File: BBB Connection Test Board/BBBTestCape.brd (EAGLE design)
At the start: 49.5 x 47.9 mm, 22 parts, among them X1 SWTCH_BLCK, X2 SWTCH_BLCK

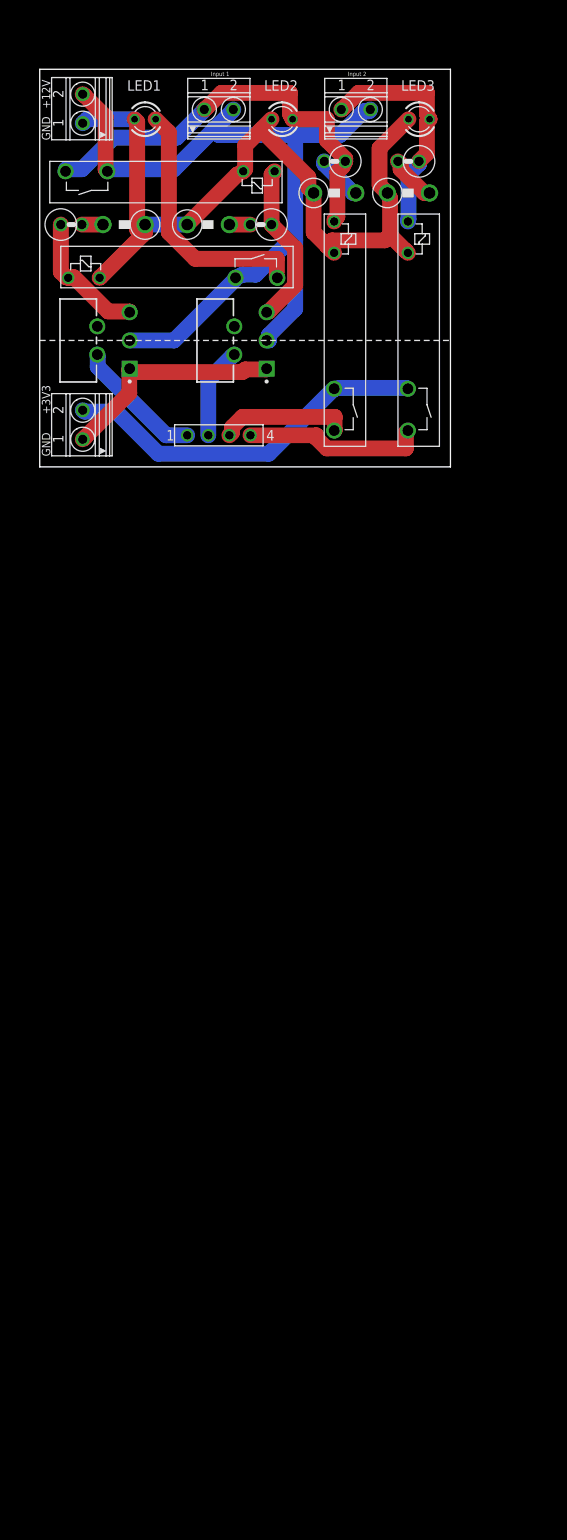
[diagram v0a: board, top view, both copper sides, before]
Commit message: WIP: Starting BBB Connection Test Board rev B. Added MCP23017
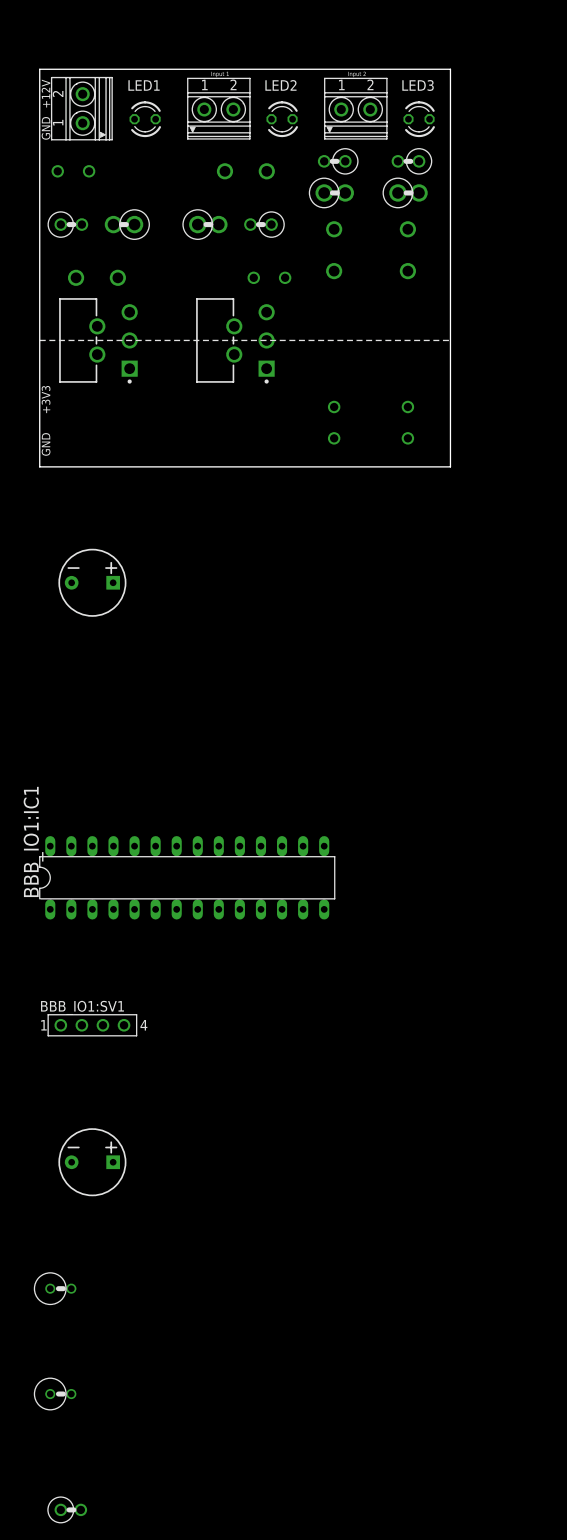
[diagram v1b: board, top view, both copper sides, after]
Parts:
- removed 3V3_PWR_BLK:PWR: PWR_BLK, relay_computer_custom:1751248
- removed SV1: (no value), relay_computer_custom:FE04-1
- added 12V_PWR_BLK:C1, BBB_IO1:C1: 100uF, relay_computer_custom:CPOL-RADIAL-5MM-8MM
- added BBB_IO1:C2: 0.1UF, relay_computer_custom:VERT_CAP
- added BBB_IO1:IC1: MCP23017SP, relay_computer_custom:DIL28-3
- added BBB_IO1:R1, BBB_IO1:R2: 4.7KOHM, relay_computer_custom:RAD2.5_RES
- added BBB_IO1:SV1: (no value), relay_computer_custom:FE04-1
- 12V_TO_3V3_1BIT1:D6, 3V3_TO_12_1BIT1:D4, DUAL_12V⇆3V3_1BIT1:12V_TO_3V3_1BIT1:D6, DUAL_12V⇆3V3_1BIT1:3V3_TO_12_1BIT1:D4: value 1N5359 -> 1N5359VERT_SML; device relay_computer_custom:C1702-05 -> relay_computer_custom:RAD2.5_D2
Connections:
- removed net BBB1: 3V3_TO_12_1BIT1:U1.2, SV1.1
- removed net BBB2: DUAL_12V⇆3V3_1BIT1:3V3_TO_12_1BIT1:U1.2, SV1.2
- removed net BBB3: DUAL_12V⇆3V3_1BIT1:12V_TO_3V3_1BIT1:K3.5, SV1.3
- removed net BBB4: 12V_TO_3V3_1BIT1:K3.5, SV1.4
- new net BBB_IO1:SCL: BBB_IO1:IC1.12, BBB_IO1:R1.C, BBB_IO1:SV1.3
- new net BBB_IO1:SDA: BBB_IO1:IC1.13, BBB_IO1:R2.C, BBB_IO1:SV1.4
- new net N$4: BBB_IO1:IC1.8, DUAL_12V⇆3V3_1BIT1:3V3_TO_12_1BIT1:U1.2
- new net N$5: BBB_IO1:IC1.1, DUAL_12V⇆3V3_1BIT1:12V_TO_3V3_1BIT1:K3.5
- new net N$6: 3V3_TO_12_1BIT1:U1.2, BBB_IO1:IC1.28
- new net N$7: 12V_TO_3V3_1BIT1:K3.5, BBB_IO1:IC1.21
- net +12V: now also 12V_PWR_BLK:C1.1
- net +3V3: now also BBB_IO1:C1.1, BBB_IO1:C2.A, BBB_IO1:IC1.18, BBB_IO1:IC1.9, BBB_IO1:R1.A, BBB_IO1:R2.A, BBB_IO1:SV1.1; no longer 3V3_PWR_BLK:PWR.2
- net GND: now also 12V_PWR_BLK:C1.2
- net GND3: now also BBB_IO1:C1.2, BBB_IO1:C2.C, BBB_IO1:IC1.10, BBB_IO1:IC1.15, BBB_IO1:IC1.16, BBB_IO1:IC1.17, BBB_IO1:SV1.2; no longer 3V3_PWR_BLK:PWR.1
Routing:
- net +12V: track 100.6 -> 0.00 mm
- net GND: track 97.2 -> 0.00 mm
- net N$3: track 52.2 -> 0.00 mm
- net +3V3: track 44.6 -> 0.00 mm
- net N$1: track 31.0 -> 0.00 mm
- net N$2: track 27.8 -> 0.00 mm
- net GND3: track 27.7 -> 0.00 mm
- net BBB4: track 21.8 -> 0.00 mm
- net DUAL_12V⇆3V3_1BIT1:3V3_TO_12_1BIT1:N$1: track 19.8 -> 0.00 mm
- net 3V3_TO_12_1BIT1:N$1: track 16.1 -> 0.00 mm
- net BBB1: track 15.7 -> 0.00 mm
- net BBB3: track 15.7 -> 0.00 mm
- net BBB2: track 11.0 -> 0.00 mm
- net 12V_TO_3V3_1BIT1:D$3: track 5.76 -> 0.00 mm
- net DUAL_12V⇆3V3_1BIT1:12V_TO_3V3_1BIT1:D$3: track 5.57 -> 0.00 mm
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
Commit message: WIP: starting layout of BBB conn. test board rev B
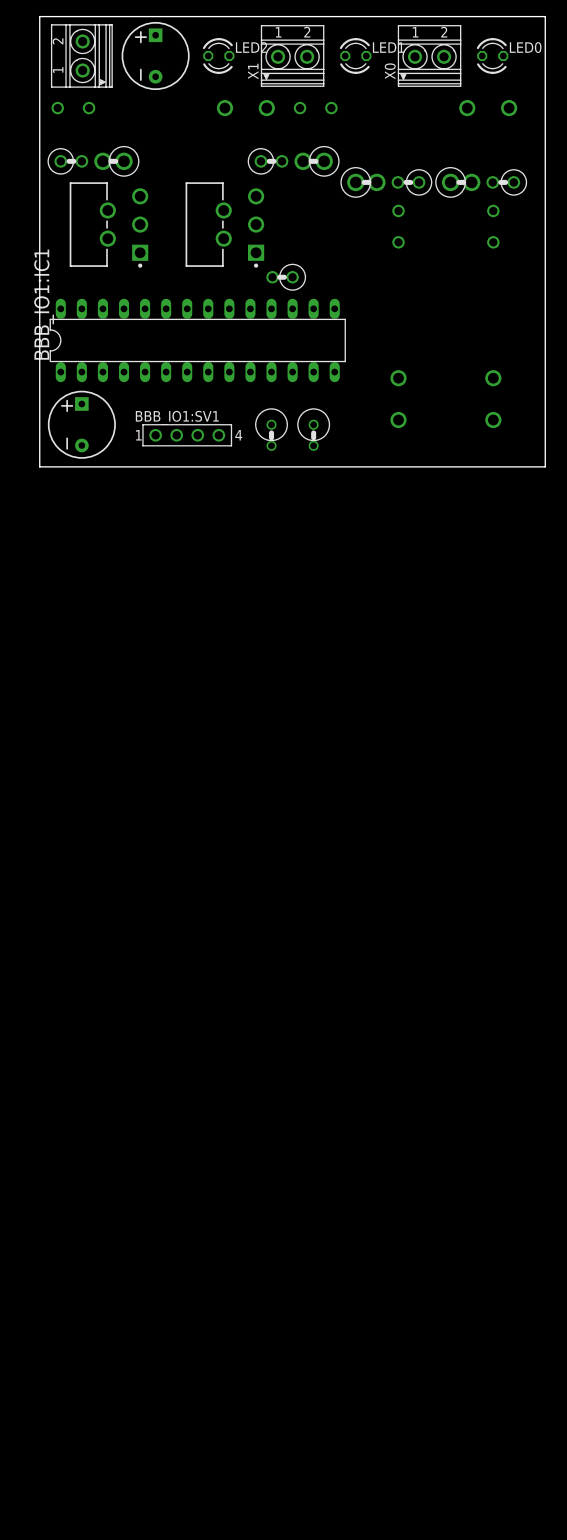
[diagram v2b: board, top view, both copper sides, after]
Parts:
- removed LED3: (no value), relay_computer_custom:LED3MM
- removed X2: SWTCH_BLCK, relay_computer_custom:1751248
- added LED0: (no value), relay_computer_custom:LED3MM
- added X0: SWTCH_BLCK, relay_computer_custom:1751248
- moved BBB_IO1:C2 150.7 mm to (29.2, 22.9), turned to 180 degrees
- moved BBB_IO1:R2 119.5 mm to (33.0, 3.81), turned to 270 degrees
- moved BBB_IO1:R1 106.0 mm to (27.9, 3.81), turned to 270 degrees
- moved BBB_IO1:C1 88.9 mm to (5.08, 5.08), turned to 90 degrees
- moved BBB_IO1:SV1 72.0 mm to (17.8, 3.81)
- moved BBB_IO1:IC1 64.8 mm to (19.1, 15.2)
- moved 12V_PWR_BLK:C1 64.0 mm to (14.0, 49.5), turned to 90 degrees
- moved 3V3_TO_12_1BIT1:K2 60.4 mm to (58.4, 44.5), turned to 180 degrees
- moved 3V3_TO_12_1BIT1:D3 41.0 mm to (44.5, 34.3), turned to 180 degrees
- moved 3V3_TO_12_1BIT1:D4 29.6 mm to (39.4, 34.3), turned to 0 degrees
- moved 12V_TO_3V3_1BIT1:K3 29.5 mm to (55.9, 3.81), turned to 90 degrees
- moved DUAL_12V⇆3V3_1BIT1:12V_TO_3V3_1BIT1:K3 28.5 mm to (44.5, 3.81), turned to 90 degrees
- moved LED1 26.5 mm to (38.1, 49.5), turned to 0 degrees
- moved DUAL_12V⇆3V3_1BIT1:3V3_TO_12_1BIT1:D3 24.1 mm to (3.81, 36.8), turned to 0 degrees
- moved 3V3_TO_12_1BIT1:U1 20.7 mm to (24.1, 29.2)
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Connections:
- net +12V: now also X0.2; no longer X2.2
- net GND: now also LED0.K; no longer LED3.K
- net N$2: now also LED0.A, X0.1; no longer LED3.A, X2.1
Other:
- board size 49.5 x 47.9 mm -> 60.9 x 54.3 mm
- board text removed: "+12V"
- board text removed: "+3V3"
- board text removed: "BBB Test Board Rev A"
- board text removed: "GND"
- board text removed: "Input 1"
- board text removed: "Input 2"

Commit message: Almost finished with Rev B of connector board. Comestic changes only
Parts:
- moved DUAL_12V⇆3V3_1BIT1:3V3_TO_12_1BIT1:D3 27.9 mm to (29.2, 25.4), turned to 180 degrees
- moved DUAL_12V⇆3V3_1BIT1:3V3_TO_12_1BIT1:D4 21.7 mm to (29.2, 29.2), turned to 0 degrees
- moved DUAL_12V⇆3V3_1BIT1:12V_TO_3V3_1BIT1:D5 14.5 mm to (36.8, 25.4)
- moved 3V3_TO_12_1BIT1:D4 13.2 mm to (47.0, 23.5), turned to 90 degrees
- moved 12V_TO_3V3_1BIT1:D6 12.5 mm to (57.1, 23.5), turned to 90 degrees
- moved DUAL_12V⇆3V3_1BIT1:12V_TO_3V3_1BIT1:D6 8.03 mm to (35.6, 29.2)
- moved 12V_PWR_BLK:C1 7.62 mm to (14.0, 41.9)
- moved 12V_PWR_BLK:PWR 7.62 mm to (5.08, 41.9)
- moved 3V3_TO_12_1BIT1:K2 7.62 mm to (58.4, 36.8)
- moved DUAL_12V⇆3V3_1BIT1:3V3_TO_12_1BIT1:K2 7.62 mm to (29.2, 36.8)
- moved LED0 7.62 mm to (54.6, 41.9), turned to 270 degrees
- moved LED1 7.62 mm to (38.1, 41.9), turned to 270 degrees
- moved LED2 7.62 mm to (21.6, 41.9), turned to 270 degrees
- moved X0 7.62 mm to (47.0, 41.9)
- moved X1 7.62 mm to (30.5, 41.9)
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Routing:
- net N$5: track 0.00 -> 45.5 mm
- net N$3: track 0.00 -> 44.9 mm
- net DUAL_12V⇆3V3_1BIT1:3V3_TO_12_1BIT1:N$1: track 0.00 -> 39.8 mm
- net N$7: track 0.00 -> 37.6 mm
- net N$4: track 0.00 -> 31.9 mm
- net 3V3_TO_12_1BIT1:N$1: track 0.00 -> 30.4 mm
- net N$6: track 0.00 -> 29.5 mm
- net N$2: track 0.00 -> 28.2 mm
- net N$1: track 0.00 -> 21.6 mm
- net BBB_IO1:SDA: track 0.00 -> 18.8 mm
- net BBB_IO1:SCL: track 0.00 -> 16.5 mm
- net DUAL_12V⇆3V3_1BIT1:12V_TO_3V3_1BIT1:D$3: track 0.00 -> 10.5 mm
- net DUAL_12V⇆3V3_1BIT1:3V3_TO_12_1BIT1:D$2: track 0.00 -> 4.86 mm
- net 3V3_TO_12_1BIT1:D$2: track 0.00 -> 2.54 mm
- net 12V_TO_3V3_1BIT1:D$3: track 0.00 -> 2.54 mm
- added copper zone on layer 15, net +12V
- added copper zone on layer 15, net +3V3
- added copper zone on layer 2, net GND
- added copper zone on layer 2, net GND3
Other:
- board size 60.9 x 54.3 mm -> 59.7 x 46.7 mm
- board text added: "12V"
- board text added: "3.3V"
- board text added: "GND"
- board text added: "SCL"
- board text added: "SDA"

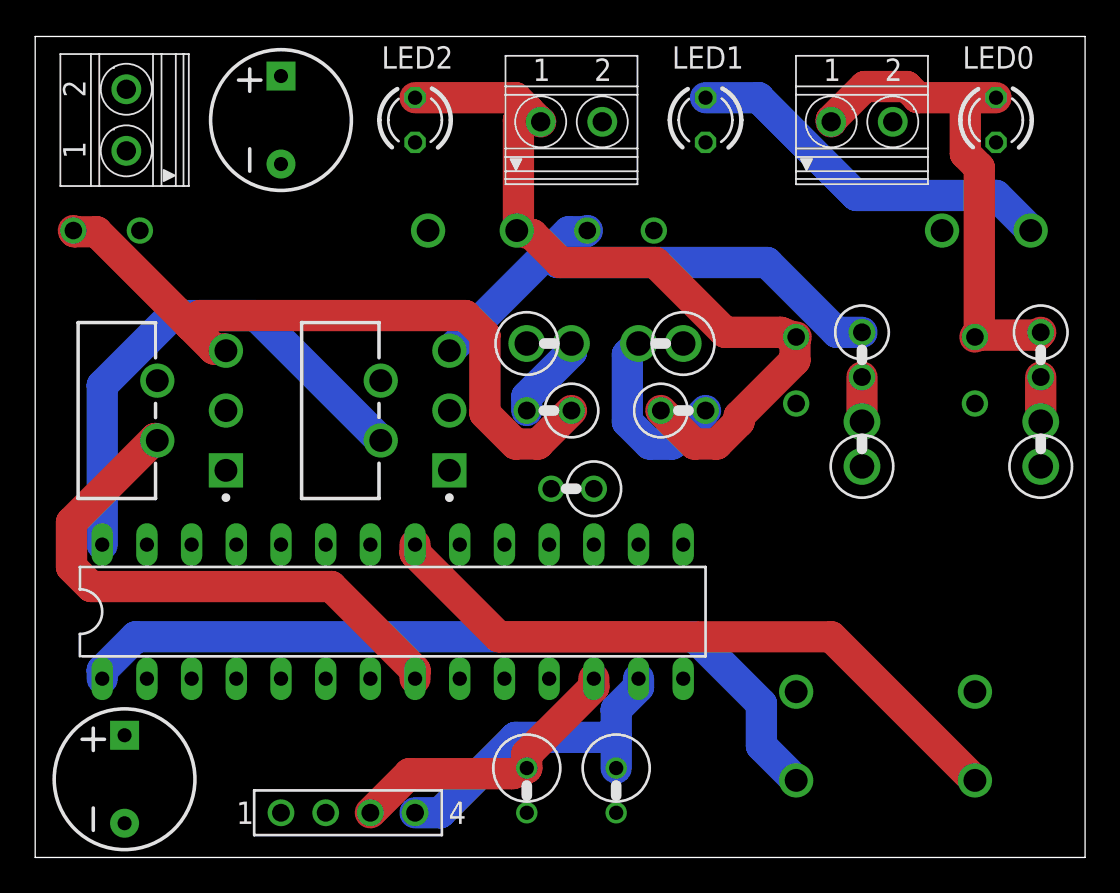
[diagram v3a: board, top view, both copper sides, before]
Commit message: Adding pull down resistors for inputs to MCP23017
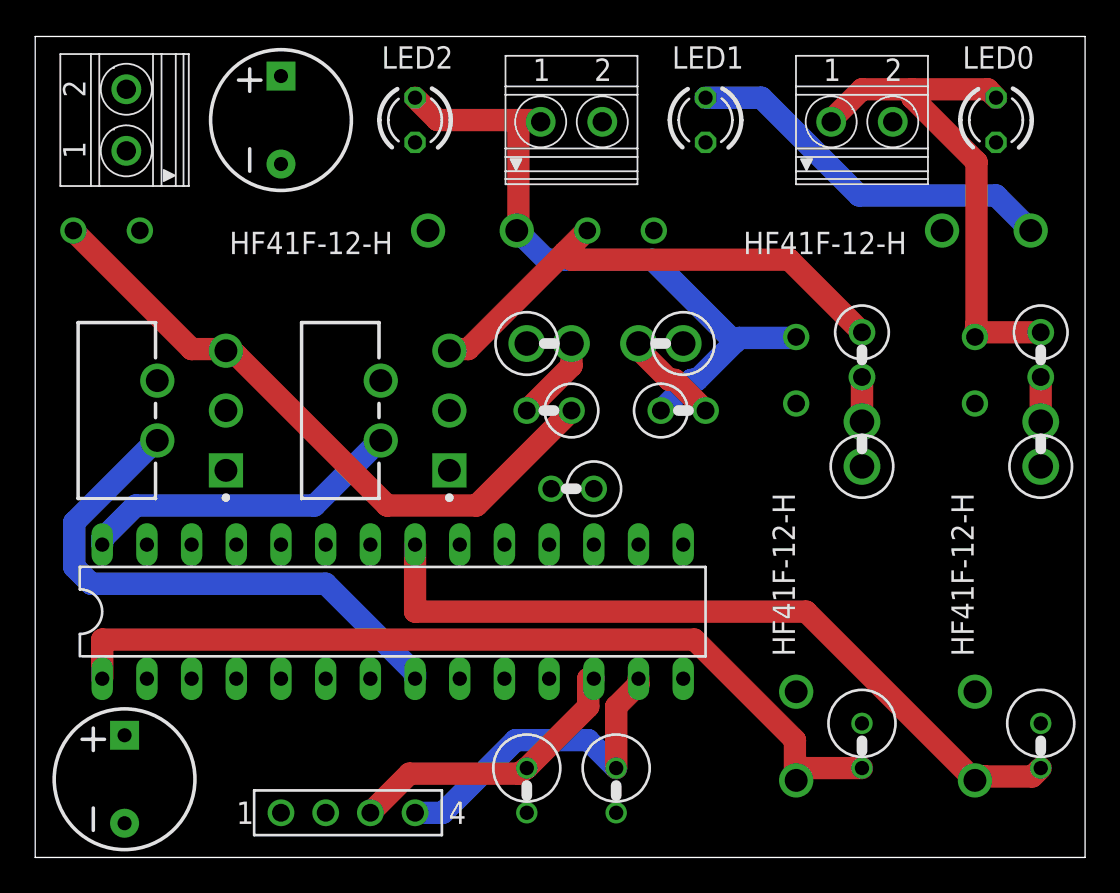
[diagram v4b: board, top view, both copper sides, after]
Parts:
- added BBB_IO1:R3, BBB_IO1:R4: 4.7KOHM, relay_computer_custom:RAD2.5_RES
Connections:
- net GND3: now also BBB_IO1:R3.C, BBB_IO1:R4.C
- net N$5: now also BBB_IO1:R4.A
- net N$7: now also BBB_IO1:R3.A
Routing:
- net N$6: track 29.5 -> 18.5 mm
- net N$3: track 44.9 -> 38.5 mm
- net N$7: track 37.6 -> 43.6 mm
- net N$5: track 45.5 -> 50.4 mm
- net DUAL_12V⇆3V3_1BIT1:12V_TO_3V3_1BIT1:D$3: track 10.5 -> 5.57 mm
- net DUAL_12V⇆3V3_1BIT1:3V3_TO_12_1BIT1:N$1: track 39.8 -> 37.0 mm
- net N$2: track 28.2 -> 29.8 mm
- net 3V3_TO_12_1BIT1:N$1: track 30.4 -> 29.4 mm
- net BBB_IO1:SDA: track 18.8 -> 19.4 mm
- net N$4: track 31.9 -> 31.4 mm

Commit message: Finishing touches of BBB Connection test Rev B board. Awaiting final review
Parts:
- moved BBB_IO1:R1 3.81 mm to (31.8, 3.81)
- moved BBB_IO1:R2 3.17 mm to (36.2, 3.81)
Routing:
- net BBB_IO1:SCL: track 16.8 -> 20.3 mm
- net BBB_IO1:SDA: track 19.4 -> 22.9 mm
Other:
- board text added: "BBB Connector Test Board Rev B"
- board text added: "JAKE KARNES"
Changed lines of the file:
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@@
 <layers>
 <layer number="1" name="Top" color="4" fill="1" visible="yes" active="yes"/>
-<layer number="2" name="Route2" color="1" fill="3" visible="no" active="yes"/>
-<layer number="15" name="Route15" color="4" fill="6" visible="no" active="yes"/>
+<layer number="2" name="Route2" color="1" fill="3" visible="yes" active="yes"/>
+<layer number="15" name="Route15" color="4" fill="6" visible="yes" active="yes"/>
 <layer number="16" name="Bottom" color="1" fill="1" visible="yes" active="yes"/>
 <layer number="17" name="Pads" color="2" fill="1" visible="yes" active="yes"/>
@@
 <text x="0.889" y="43.815" size="0.6096" layer="51" rot="R90">12V</text>
 <text x="0.889" y="39.37" size="0.6096" layer="51" rot="R90">GND</text>
+<text x="49.53" y="37.465" size="1.778" layer="26" rot="MR0">BBB Connector Test Board Rev B</text>
+<text x="59.055" y="0" size="1.778" layer="26" rot="MR0">JAKE KARNES</text>
 </plain>
 <attributes>
@@
 <attribute name="VALUE" x="4.572" y="13.0302" size="1.778" layer="27" ratio="10"/>
 </element>
-<element name="BBB_IO1:R1" library="relay_computer_custom" package="RAD2.5_RES" value="4.7KOHM" x="27.94" y="3.81" rot="R270"/>
-<element name="BBB_IO1:R2" library="relay_computer_custom" package="RAD2.5_RES" value="4.7KOHM" x="33.02" y="3.81" rot="R270"/>
+<element name="BBB_IO1:R1" library="relay_computer_custom" package="RAD2.5_RES" value="4.7KOHM" x="31.75" y="3.81" rot="R270"/>
+<element name="BBB_IO1:R2" library="relay_computer_custom" package="RAD2.5_RES" value="4.7KOHM" x="36.195" y="3.81" rot="R270"/>
 <element name="BBB_IO1:SV1" library="relay_computer_custom" package="FE04-1" value="" x="17.78" y="2.54" smashed="yes">
 <attribute name="MF" value="Sullins Connector Solutions" x="17.78" y="2.54" size="1.778" layer="27" display="off"/>
@@
 <contactref element="12V_TO_3V3_1BIT1:K3" pad="2"/>
 <contactref element="DUAL_12V⇆3V3_1BIT1:12V_TO_3V3_1BIT1:K3" pad="2"/>
-<polygon width="0.1524" layer="2">
+<polygon width="0.1524" layer="2" isolate="0.254">
 <vertex x="0" y="46.355"/>
 <vertex x="59.69" y="46.355"/>
@@
 <contactref element="12V_PWR_BLK:PWR" pad="2"/>
 <contactref element="12V_PWR_BLK:C1" pad="1"/>
-<polygon width="0.1524" layer="15">
+<polygon width="0.1524" layer="15" isolate="0.254">
 <vertex x="59.69" y="19.685"/>
 <vertex x="59.69" y="46.355"/>
@@
 <contactref element="BBB_IO1:IC1" pad="16"/>
 <contactref element="BBB_IO1:C2" pad="C"/>
-<polygon width="0.1524" layer="2">
+<polygon width="0.1524" layer="2" isolate="0.254">
 <vertex x="0" y="22.225"/>
 <vertex x="35.56" y="22.225"/>
@@
 <contactref element="BBB_IO1:R2" pad="A"/>
 <contactref element="BBB_IO1:C2" pad="A"/>
-<polygon width="0.1524" layer="15">
+<polygon width="0.1524" layer="15" isolate="0.254">
 <vertex x="0.635" y="22.225"/>
 <vertex x="35.56" y="22.225"/>
@@
 <contactref element="BBB_IO1:IC1" pad="12"/>
 <contactref element="BBB_IO1:R1" pad="C"/>
-<wire x1="31.4325" y1="8.5725" x2="27.94" y2="5.08" width="1.27" layer="1"/>
-<wire x1="31.4325" y1="10.16" x2="31.4325" y2="8.5725" width="1.27" layer="1"/>
-<wire x1="31.75" y1="10.16" x2="31.4325" y2="10.16" width="1.27" layer="1"/>
-<wire x1="21.2725" y1="4.7625" x2="19.05" y2="2.54" width="1.27" layer="1"/>
-<wire x1="27.46375" y1="4.7625" x2="21.2725" y2="4.7625" width="1.27" layer="1"/>
-<wire x1="27.46375" y1="4.7625" x2="27.94" y2="5.08" width="1.27" layer="1"/>
+<wire x1="31.75" y1="5.08" x2="19.05" y2="5.08" width="1.524" layer="1"/>
+<wire x1="31.75" y1="10.16" x2="31.75" y2="5.08" width="1.524" layer="1"/>
+<wire x1="19.05" y1="5.08" x2="19.05" y2="2.54" width="1.524" layer="1"/>
 </signal>
 <signal name="BBB_IO1:SDA">
@@
 <contactref element="BBB_IO1:IC1" pad="13"/>
 <contactref element="BBB_IO1:R2" pad="C"/>
-<wire x1="33.02" y1="8.5725" x2="33.02" y2="5.08" width="1.27" layer="1"/>
-<wire x1="34.29" y1="9.8425" x2="33.02" y2="8.5725" width="1.27" layer="1"/>
-<wire x1="34.29" y1="10.16" x2="34.29" y2="9.8425" width="1.27" layer="1"/>
-<wire x1="23.1775" y1="2.54" x2="21.59" y2="2.54" width="1.27" layer="16"/>
-<wire x1="27.305" y1="6.6675" x2="23.1775" y2="2.54" width="1.27" layer="16"/>
-<wire x1="31.4325" y1="6.6675" x2="27.305" y2="6.6675" width="1.27" layer="16"/>
-<wire x1="33.02" y1="5.08" x2="31.4325" y2="6.6675" width="1.27" layer="16"/>
+<wire x1="34.29" y1="10.16" x2="34.29" y2="6.985" width="1.524" layer="16"/>
+<wire x1="34.29" y1="6.985" x2="36.195" y2="5.08" width="1.524" layer="16"/>
+<wire x1="31.12925625" y1="1.0414" x2="32.37074375" y2="1.0414" width="1.27" layer="16"/>
+<wire x1="32.37074375" y1="1.0414" x2="33.2486" y2="1.91925625" width="1.27" layer="16"/>
+<wire x1="21.59" y1="2.54" x2="29.63065625" y2="2.54" width="1.27" layer="16"/>
+<wire x1="33.2486" y1="1.91925625" x2="33.2486" y2="2.1336" width="1.27" layer="16"/>
+<wire x1="29.63065625" y1="2.54" x2="31.12925625" y2="1.0414" width="1.27" layer="16"/>
+<wire x1="33.2486" y1="2.1336" x2="36.195" y2="5.08" width="1.27" layer="16"/>
 </signal>
 </signals>
